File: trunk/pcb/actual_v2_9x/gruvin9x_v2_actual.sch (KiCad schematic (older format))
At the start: 140 parts, among them P2 CONN_5, P3 CONN_6, P4 CONN_9, P5 CONN_9, P6 CONN_6, P7 CONN_12, P8 CONN_30, Q1 2SC9014, SW1 SW_PUSH, SW2 SW_PUSH, SW3 SW_PUSH, SW4 SW_PUSH, SW5 SW_PUSH, SW6 SW_PUSH, U1 78L05, U2 4066, U3 LN-6206-30, X1 16MHz

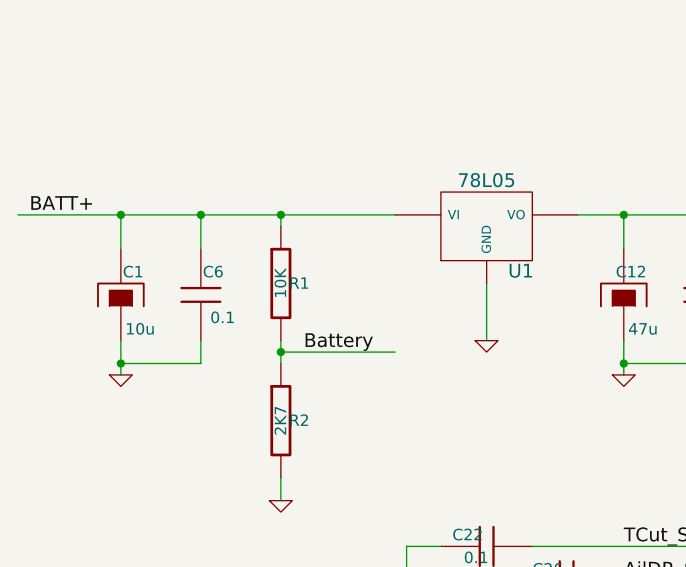
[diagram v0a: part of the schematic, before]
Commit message: Added Turnigy 9X V2 backup firmware to allow restoring of original V2 factory firmware. (This firmware as supplied by http://HobbyKing.com)
Corrected error in all circuit schematic versiosn -- R1 is a 5K1, not a 10K.
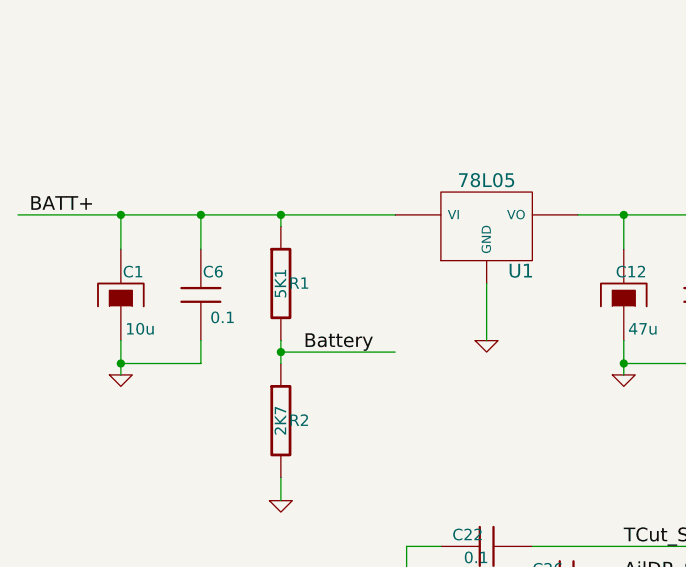
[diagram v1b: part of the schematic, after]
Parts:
- R1: value 10K -> 5K1
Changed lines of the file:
@@
-EESchema Schematic File Version 2  date 1/12/2010 4:57:59 p.m.
+EESchema Schematic File Version 2  date 14/12/2010 1:54:23 p.m.
 LIBS:power
 LIBS:device
@@
 Sheet 1 1
 Title "Main Controller PCB (Stock)"
-Date "1 dec 2010"
+Date "14 dec 2010"
 Rev "1.1"
 Comp "gruvin9x"
@@
 P 1750 1250
 F 0 "R1" H 1830 1250 50  0000 C CNN
-F 1 "10K" V 1750 1250 50  0000 C CNN
+F 1 "5K1" V 1750 1250 50  0000 C CNN
 	1    1750 1250
 	1    0    0    -1

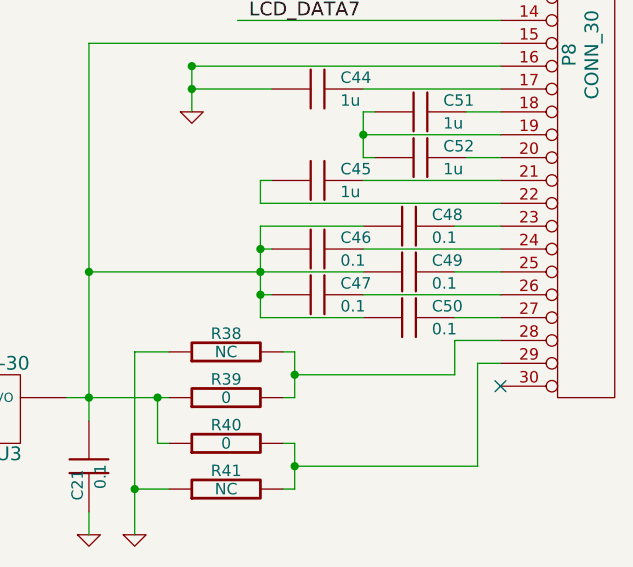
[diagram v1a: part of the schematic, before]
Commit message: PCB V3 re-routed to corrected V3 schematic (trims + PPM-in inverting buffer). Corrections made to LCD decoupling capacitor values (1uF) on other schematics.
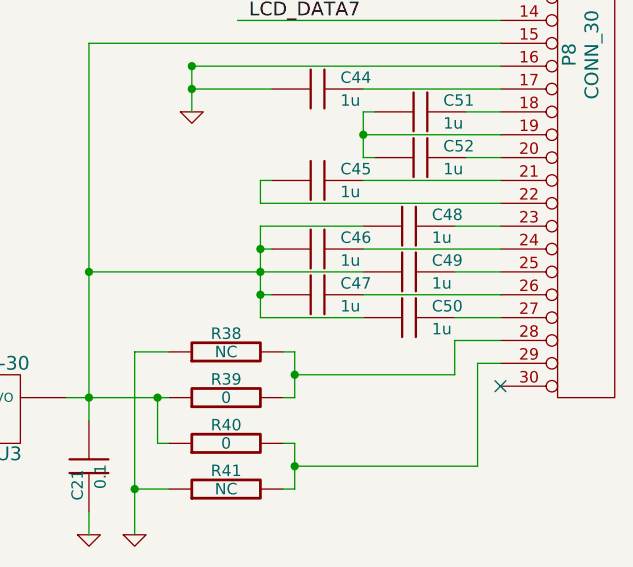
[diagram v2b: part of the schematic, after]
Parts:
- C46, C47, C48, C49, C50: value 0.1 -> 1u
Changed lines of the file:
@@
-EESchema Schematic File Version 2  date 14/12/2010 1:54:23 p.m.
+EESchema Schematic File Version 2  date 14/01/2011 12:17:27 p.m.
 LIBS:power
 LIBS:device
@@
 Sheet 1 1
 Title "Main Controller PCB (Stock)"
-Date "14 dec 2010"
-Rev "1.1"
+Date "13 jan 2011"
+Rev "1.2"
 Comp "gruvin9x"
 Comment1 "(Layout designed to suit easy conversion to 2xA4 if required.)"
@@
 P 14700 3600
 F 0 "C50" V 14650 3700 50  0000 L CNN
-F 1 "0.1" V 14750 3700 50  0000 L CNN
+F 1 "1u" V 14750 3700 50  0000 L CNN
 	1    14700 3600
 	0    1    1    0
@@
 P 14300 3500
 F 0 "C47" V 14250 3600 50  0000 L CNN
-F 1 "0.1" V 14350 3600 50  0000 L CNN
+F 1 "1u" V 14350 3600 50  0000 L CNN
 	1    14300 3500
 	0    1    1    0
@@
 P 14300 3300
 F 0 "C46" V 14250 3400 50  0000 L CNN
-F 1 "0.1" V 14350 3400 50  0000 L CNN
+F 1 "1u" V 14350 3400 50  0000 L CNN
 	1    14300 3300
 	0    1    1    0
@@
 P 14700 3400
 F 0 "C49" V 14650 3500 50  0000 L CNN
-F 1 "0.1" V 14750 3500 50  0000 L CNN
+F 1 "1u" V 14750 3500 50  0000 L CNN
 	1    14700 3400
 	0    1    1    0
@@
 P 14700 3200
 F 0 "C48" V 14650 3300 50  0000 L CNN
-F 1 "0.1" V 14750 3300 50  0000 L CNN
+F 1 "1u" V 14750 3300 50  0000 L CNN
 	1    14700 3200
 	0    1    1    0

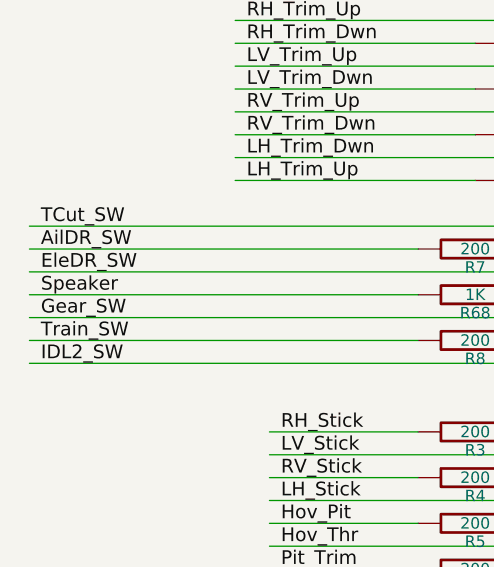
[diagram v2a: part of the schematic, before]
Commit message: PCB V3.3 updated. Includes changes to SD card connector and interface board, which now includes the I2C Real Time Clock chip.
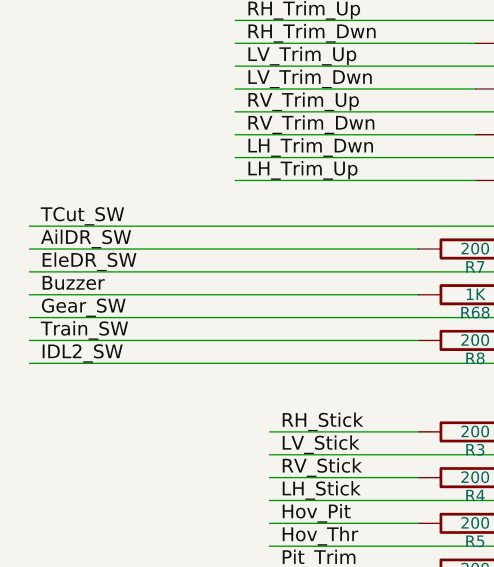
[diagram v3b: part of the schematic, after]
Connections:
- net labels added: Buzzer
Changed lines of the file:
@@
-EESchema Schematic File Version 2  date 14/01/2011 12:17:27 p.m.
+EESchema Schematic File Version 2  date 25/01/2011 3:32:26 p.m.
 LIBS:power
 LIBS:device
@@
 Sheet 1 1
 Title "Main Controller PCB (Stock)"
-Date "13 jan 2011"
+Date "25 jan 2011"
 Rev "1.2"
 Comp "gruvin9x"
@@
 TCut_SW
 Text Label 700  8500 0    60   ~ 0
-Speaker
+Buzzer
 $Comp
 L R R26
